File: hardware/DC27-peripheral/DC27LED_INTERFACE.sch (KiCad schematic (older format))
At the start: 16 parts, among them U2 IS31FL736

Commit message: commit the current hardware files
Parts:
- C1, C2, C3, C4, C5, C6, C7, C8, C9: footprint (none) -> Capacitor_SMD:C_0603_1608Metric
- R1, R2, R3, R4, R5, R6: footprint (none) -> Resistor_SMD:R_0603_1608Metric
- U2: footprint Package_DFN_QFN:QFN-40-1EP_4x4mm_P0.4mm_EP2.4x2.4mm -> dc27-sao-extras:QFN-40-1EP_5x5mm_P0.4mm_EP3.5x3.5mm
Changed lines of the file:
@@
 EESchema Schematic File Version 4
-LIBS:DC27-peripheral-cache
+LIBS:DC27-badge-cache
 EELAYER 26 0
 EELAYER END
@@
 F 0 "U2" H 5750 3450 50  0000 C CNN
 F 1 "IS31FL736" H 5750 3300 50  0000 C CNN
-F 2 "Package_DFN_QFN:QFN-40-1EP_4x4mm_P0.4mm_EP2.4x2.4mm" H 5700 1600 50  0001 C CNN
+F 2 "dc27-sao-extras:QFN-40-1EP_5x5mm_P0.4mm_EP3.5x3.5mm" H 5700 1600 50  0001 C CNN
 F 3 "http://www.issi.com/WW/pdf/IS31FL3216.pdf" H 4120 4590 50  0001 C CNN
 	1    5750 3450
@@
 F 0 "C1" H 2215 1496 50  0000 L CNN
 F 1 "0.47uF" H 2215 1405 50  0000 L CNN
-F 2 "" H 2138 1300 50  0001 C CNN
+F 2 "Capacitor_SMD:C_0603_1608Metric" H 2138 1300 50  0001 C CNN
 F 3 "~" H 2100 1450 50  0001 C CNN
 	1    2100 1450
@@
 F 0 "C2" H 2815 1496 50  0000 L CNN
 F 1 "0.1uF" H 2815 1405 50  0000 L CNN
-F 2 "" H 2738 1300 50  0001 C CNN
+F 2 "Capacitor_SMD:C_0603_1608Metric" H 2738 1300 50  0001 C CNN
 F 3 "~" H 2700 1450 50  0001 C CNN
 	1    2700 1450
@@
 F 0 "C3" H 2215 2496 50  0000 L CNN
 F 1 "0.47uF" H 2215 2405 50  0000 L CNN
-F 2 "" H 2138 2300 50  0001 C CNN
+F 2 "Capacitor_SMD:C_0603_1608Metric" H 2138 2300 50  0001 C CNN
 F 3 "~" H 2100 2450 50  0001 C CNN
 	1    2100 2450
@@
 F 0 "C4" H 2815 2496 50  0000 L CNN
 F 1 "0.1uF" H 2815 2405 50  0000 L CNN
-F 2 "" H 2738 2300 50  0001 C CNN
+F 2 "Capacitor_SMD:C_0603_1608Metric" H 2738 2300 50  0001 C CNN
 F 3 "~" H 2700 2450 50  0001 C CNN
 	1    2700 2450
@@
 F 0 "C5" H 2215 3496 50  0000 L CNN
 F 1 "0.47uF" H 2215 3405 50  0000 L CNN
-F 2 "" H 2138 3300 50  0001 C CNN
+F 2 "Capacitor_SMD:C_0603_1608Metric" H 2138 3300 50  0001 C CNN
 F 3 "~" H 2100 3450 50  0001 C CNN
 	1    2100 3450
@@
 F 0 "C6" H 2815 3496 50  0000 L CNN
 F 1 "0.1uF" H 2815 3405 50  0000 L CNN
-F 2 "" H 2738 3300 50  0001 C CNN
+F 2 "Capacitor_SMD:C_0603_1608Metric" H 2738 3300 50  0001 C CNN
 F 3 "~" H 2700 3450 50  0001 C CNN
 	1    2700 3450
@@
 F 0 "C7" H 2215 4496 50  0000 L CNN
 F 1 "0.47uF" H 2215 4405 50  0000 L CNN
-F 2 "" H 2138 4300 50  0001 C CNN
+F 2 "Capacitor_SMD:C_0603_1608Metric" H 2138 4300 50  0001 C CNN
 F 3 "~" H 2100 4450 50  0001 C CNN
 	1    2100 4450
@@
 F 0 "C8" H 2815 4496 50  0000 L CNN
 F 1 "0.1uF" H 2815 4405 50  0000 L CNN
-F 2 "" H 2738 4300 50  0001 C CNN
+F 2 "Capacitor_SMD:C_0603_1608Metric" H 2738 4300 50  0001 C CNN
 F 3 "~" H 2700 4450 50  0001 C CNN
 	1    2700 4450
@@
 F 0 "R5" V 7200 4250 50  0000 C CNN
 F 1 "20K" V 7300 4250 50  0000 C CNN
-F 2 "" V 7140 4240 50  0001 C CNN
+F 2 "Resistor_SMD:R_0603_1608Metric" V 7140 4240 50  0001 C CNN
 F 3 "~" H 7100 4250 50  0001 C CNN
 	1    7100 4250
@@
 F 0 "C9" H 2215 5546 50  0000 L CNN
 F 1 "C" H 2215 5455 50  0000 L CNN
-F 2 "" H 2138 5350 50  0001 C CNN
+F 2 "Capacitor_SMD:C_0603_1608Metric" H 2138 5350 50  0001 C CNN
 F 3 "~" H 2100 5500 50  0001 C CNN
 	1    2100 5500
@@
 F 0 "R6" H 5168 5196 50  0000 L CNN
 F 1 "100k" H 5168 5105 50  0000 L CNN
-F 2 "" V 5030 5150 50  0001 C CNN
+F 2 "Resistor_SMD:R_0603_1608Metric" V 5030 5150 50  0001 C CNN
 F 3 "~" H 5100 5150 50  0001 C CNN
 	1    5100 5150
@@
 F 0 "R1" H 8770 1496 50  0000 L CNN
 F 1 "100k" H 8770 1405 50  0000 L CNN
-F 2 "" V 8630 1450 50  0001 C CNN
+F 2 "Resistor_SMD:R_0603_1608Metric" V 8630 1450 50  0001 C CNN
 F 3 "~" H 8700 1450 50  0001 C CNN
 	1    8700 1450
@@
 F 0 "R2" H 9120 1496 50  0000 L CNN
 F 1 "1k" H 9120 1405 50  0000 L CNN
-F 2 "" V 8980 1450 50  0001 C CNN
+F 2 "Resistor_SMD:R_0603_1608Metric" V 8980 1450 50  0001 C CNN
 F 3 "~" H 9050 1450 50  0001 C CNN
 	1    9050 1450
@@
 F 0 "R3" H 9520 1496 50  0000 L CNN
 F 1 "1k" H 9520 1405 50  0000 L CNN
-F 2 "" V 9380 1450 50  0001 C CNN
+F 2 "Resistor_SMD:R_0603_1608Metric" V 9380 1450 50  0001 C CNN
 F 3 "~" H 9450 1450 50  0001 C CNN
 	1    9450 1450
@@
 F 0 "R4" H 9120 2996 50  0000 L CNN
 F 1 "100k" H 9120 2905 50  0000 L CNN
-F 2 "" V 8980 2950 50  0001 C CNN
+F 2 "Resistor_SMD:R_0603_1608Metric" V 8980 2950 50  0001 C CNN
 F 3 "~" H 9050 2950 50  0001 C CNN
 	1    9050 2950

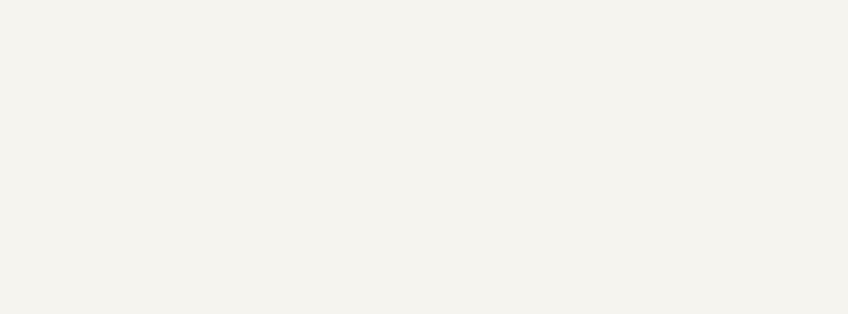
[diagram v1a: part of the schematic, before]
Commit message: Clean up SPI bus, set correct pins, start working through DRC errors.
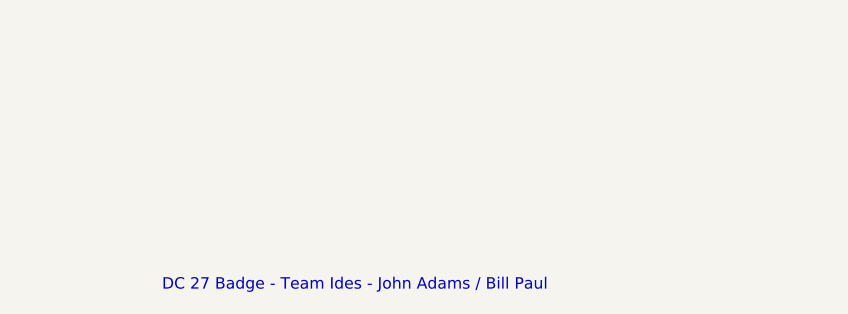
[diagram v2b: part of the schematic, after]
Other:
- note added: "DC 27 Badge - Team Ides - John Adams / Bill Paul"
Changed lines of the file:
@@
 Wire Wire Line
 	2100 5200 2700 5200
+Text Notes 7350 7500 0    50   ~ 0
+DC 27 Badge - Team Ides - John Adams / Bill Paul
 $EndSCHEMATC

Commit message: checkpoint all of the kicad stuff
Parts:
- renumbered C6 to C10, C7 to C11, C8 to C12, C9 to C13, C1 to C5, C2 to C6, C3 to C7, C4 to C8, C5 to C9, R1 to R3, R2 to R4, R3 to R5, R4 to R6, R5 to R7, R6 to R8, U2 to U3
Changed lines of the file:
@@
 $Descr A4 11693 8268
 encoding utf-8
-Sheet 3 5
+Sheet 3 6
 Title ""
 Date ""
@@
 P 5750 3450
 AR Path="/5BA1B02E/5BD866E6" Ref="U?"  Part="1"
-AR Path="/5BD866AF/5BD866E6" Ref="U2"  Part="1"
-F 0 "U2" H 5750 3450 50  0000 C CNN
+AR Path="/5BD866AF/5BD866E6" Ref="U3"  Part="1"
+F 0 "U3" H 5750 3450 50  0000 C CNN
 F 1 "IS31FL736" H 5750 3300 50  0000 C CNN
 F 2 "dc27-sao-extras:QFN-40-1EP_5x5mm_P0.4mm_EP3.5x3.5mm" H 5700 1600 50  0001 C CNN
@@
 VCC5V
 $Comp
-L Device:C C1
+L Device:C C5
 U 1 1 5BDAD420
 P 2100 1450
-F 0 "C1" H 2215 1496 50  0000 L CNN
+F 0 "C5" H 2215 1496 50  0000 L CNN
 F 1 "0.47uF" H 2215 1405 50  0000 L CNN
 F 2 "Capacitor_SMD:C_0603_1608Metric" H 2138 1300 50  0001 C CNN
@@
 $EndComp
 $Comp
-L Device:C C2
+L Device:C C6
 U 1 1 5BDAD49F
 P 2700 1450
-F 0 "C2" H 2815 1496 50  0000 L CNN
+F 0 "C6" H 2815 1496 50  0000 L CNN
 F 1 "0.1uF" H 2815 1405 50  0000 L CNN
 F 2 "Capacitor_SMD:C_0603_1608Metric" H 2738 1300 50  0001 C CNN
@@
 Connection ~ 2100 1250
 $Comp
-L power:GND #PWR04
+L power:GND #PWR017
 U 1 1 5BDADD7C
 P 2100 1800
-F 0 "#PWR04" H 2100 1550 50  0001 C CNN
+F 0 "#PWR017" H 2100 1550 50  0001 C CNN
 F 1 "GND" H 2105 1627 50  0000 C CNN
 F 2 "" H 2100 1800 50  0001 C CNN
@@
 $EndComp
 $Comp
-L power:GND #PWR05
+L power:GND #PWR018
 U 1 1 5BDADD94
 P 2700 1800
-F 0 "#PWR05" H 2700 1550 50  0001 C CNN
+F 0 "#PWR018" H 2700 1550 50  0001 C CNN
 F 1 "GND" H 2705 1627 50  0000 C CNN
 F 2 "" H 2700 1800 50  0001 C CNN
@@
 VCC5V
 $Comp
-L Device:C C3
+L Device:C C7
 U 1 1 5BDAF5E8
 P 2100 2450
-F 0 "C3" H 2215 2496 50  0000 L CNN
+F 0 "C7" H 2215 2496 50  0000 L CNN
 F 1 "0.47uF" H 2215 2405 50  0000 L CNN
 F 2 "Capacitor_SMD:C_0603_1608Metric" H 2138 2300 50  0001 C CNN
@@
 $EndComp
 $Comp
-L Device:C C4
+L Device:C C8
 U 1 1 5BDAF5EE
 P 2700 2450
-F 0 "C4" H 2815 2496 50  0000 L CNN
+F 0 "C8" H 2815 2496 50  0000 L CNN
 F 1 "0.1uF" H 2815 2405 50  0000 L CNN
 F 2 "Capacitor_SMD:C_0603_1608Metric" H 2738 2300 50  0001 C CNN
@@
 Connection ~ 2100 2250
 $Comp
-L power:GND #PWR06
+L power:GND #PWR019
 U 1 1 5BDAF5F9
 P 2100 2800
-F 0 "#PWR06" H 2100 2550 50  0001 C CNN
+F 0 "#PWR019" H 2100 2550 50  0001 C CNN
 F 1 "GND" H 2105 2627 50  0000 C CNN
 F 2 "" H 2100 2800 50  0001 C CNN
@@
 $EndComp
 $Comp
-L power:GND #PWR07
+L power:GND #PWR020
 U 1 1 5BDAF5FF
 P 2700 2800
-F 0 "#PWR07" H 2700 2550 50  0001 C CNN
+F 0 "#PWR020" H 2700 2550 50  0001 C CNN
 F 1 "GND" H 2705 2627 50  0000 C CNN
 F 2 "" H 2700 2800 50  0001 C CNN
@@
 VCC5V
 $Comp
-L Device:C C5
+L Device:C C9
 U 1 1 5BDAFD53
 P 2100 3450
-F 0 "C5" H 2215 3496 50  0000 L CNN
+F 0 "C9" H 2215 3496 50  0000 L CNN
 F 1 "0.47uF" H 2215 3405 50  0000 L CNN
 F 2 "Capacitor_SMD:C_0603_1608Metric" H 2138 3300 50  0001 C CNN
@@
 $EndComp
 $Comp
-L Device:C C6
+L Device:C C10
 U 1 1 5BDAFD59
 P 2700 3450
-F 0 "C6" H 2815 3496 50  0000 L CNN
+F 0 "C10" H 2815 3496 50  0000 L CNN
 F 1 "0.1uF" H 2815 3405 50  0000 L CNN
 F 2 "Capacitor_SMD:C_0603_1608Metric" H 2738 3300 50  0001 C CNN
@@
 Connection ~ 2100 3250
 $Comp
-L power:GND #PWR09
+L power:GND #PWR022
 U 1 1 5BDAFD64
 P 2100 3800
-F 0 "#PWR09" H 2100 3550 50  0001 C CNN
+F 0 "#PWR022" H 2100 3550 50  0001 C CNN
 F 1 "GND" H 2105 3627 50  0000 C CNN
 F 2 "" H 2100 3800 50  0001 C CNN
@@
 $EndComp
 $Comp
-L power:GND #PWR010
+L power:GND #PWR023
 U 1 1 5BDAFD6A
 P 2700 3800
-F 0 "#PWR010" H 2700 3550 50  0001 C CNN
+F 0 "#PWR023" H 2700 3550 50  0001 C CNN
 F 1 "GND" H 2705 3627 50  0000 C CNN
 F 2 "" H 2700 3800 50  0001 C CNN
@@
 VCC5V
 $Comp
-L Device:C C7
+L Device:C C11
 U 1 1 5BDAFD76
 P 2100 4450
-F 0 "C7" H 2215 4496 50  0000 L CNN
+F 0 "C11" H 2215 4496 50  0000 L CNN
 F 1 "0.47uF" H 2215 4405 50  0000 L CNN
 F 2 "Capacitor_SMD:C_0603_1608Metric" H 2138 4300 50  0001 C CNN
@@
 $EndComp
 $Comp
-L Device:C C8
+L Device:C C12
 U 1 1 5BDAFD7C
 P 2700 4450
-F 0 "C8" H 2815 4496 50  0000 L CNN
+F 0 "C12" H 2815 4496 50  0000 L CNN
 F 1 "0.1uF" H 2815 4405 50  0000 L CNN
 F 2 "Capacitor_SMD:C_0603_1608Metric" H 2738 4300 50  0001 C CNN
@@
 Connection ~ 2100 4250
 $Comp
-L power:GND #PWR012
+L power:GND #PWR025
 U 1 1 5BDAFD87
 P 2100 4800
-F 0 "#PWR012" H 2100 4550 50  0001 C CNN
+F 0 "#PWR025" H 2100 4550 50  0001 C CNN
 F 1 "GND" H 2105 4627 50  0000 C CNN
 F 2 "" H 2100 4800 50  0001 C CNN
@@
 $EndComp
 $Comp
-L power:GND #PWR013
+L power:GND #PWR026
 U 1 1 5BDAFD8D
 P 2700 4800
-F 0 "#PWR013" H 2700 4550 50  0001 C CNN
+F 0 "#PWR026" H 2700 4550 50  0001 C CNN
 F 1 "GND" H 2705 4627 50  0000 C CNN
 F 2 "" H 2700 4800 50  0001 C CNN
@@
 	5650 1850 5650 2100
 $Comp
-L power:GND #PWR03
+L power:GND #PWR016
 U 1 1 5BDB2F4A
 P 6050 1150
-F 0 "#PWR03" H 6050 900 50  0001 C CNN
+F 0 "#PWR016" H 6050 900 50  0001 C CNN
 F 1 "GND" H 6055 977 50  0000 C CNN
 F 2 "" H 6050 1150 50  0001 C CNN
@@
 	5950 1900 5950 2100
 $Comp
-L Device:R_US R5
+L Device:R_US R7
 U 1 1 5BDB589A
 P 7100 4250
-F 0 "R5" V 7200 4250 50  0000 C CNN
+F 0 "R7" V 7200 4250 50  0000 C CNN
 F 1 "20K" V 7300 4250 50  0000 C CNN
 F 2 "Resistor_SMD:R_0603_1608Metric" V 7140 4240 50  0001 C CNN
@@
 	6800 4250 6950 4250
 $Comp
-L power:GND #PWR011
+L power:GND #PWR024
 U 1 1 5BDB67EB
 P 7450 4300
-F 0 "#PWR011" H 7450 4050 50  0001 C CNN
+F 0 "#PWR024" H 7450 4050 50  0001 C CNN
 F 1 "GND" H 7455 4127 50  0000 C CNN
 F 2 "" H 7450 4300 50  0001 C CNN
@@
 VCC3V3
 $Comp
-L Device:C C9
+L Device:C C13
 U 1 1 5BDB89D2
 P 2100 5500
-F 0 "C9" H 2215 5546 50  0000 L CNN
+F 0 "C13" H 2215 5546 50  0000 L CNN
 F 1 "C" H 2215 5455 50  0000 L CNN
 F 2 "Capacitor_SMD:C_0603_1608Metric" H 2138 5350 50  0001 C CNN
@@
 $EndComp
 $Comp
-L power:GND #PWR015
+L power:GND #PWR028
 U 1 1 5BDB8A02
 P 2100 5750
-F 0 "#PWR015" H 2100 5500 50  0001 C CNN
+F 0 "#PWR028" H 2100 5500 50  0001 C CNN
 F 1 "GND" H 2105 5577 50  0000 C CNN
 F 2 "" H 2100 5750 50  0001 C CNN
@@
 NoConn ~ 6800 3150
 $Comp
-L power:GND #PWR014
+L power:GND #PWR027
 U 1 1 5BDBBD80
 P 5600 5600
-F 0 "#PWR014" H 5600 5350 50  0001 C CNN
+F 0 "#PWR027" H 5600 5350 50  0001 C CNN
 F 1 "GND" H 5605 5427 50  0000 C CNN
 F 2 "" H 5600 5600 50  0001 C CNN
@@
 Connection ~ 6000 5200
 $Comp
-L Device:R_US R6
+L Device:R_US R8
 U 1 1 5BDBF4DB
 P 5100 5150
-F 0 "R6" H 5168 5196 50  0000 L CNN
+F 0 "R8" H 5168 5196 50  0000 L CNN
 F 1 "100k" H 5168 5105 50  0000 L CNN
 F 2 "Resistor_SMD:R_0603_1608Metric" V 5030 5150 50  0001 C CNN
@@
 VCC3V3
 $Comp
-L Device:R R1
+L Device:R R3
 U 1 1 5BDEF0A9
 P 8700 1450
-F 0 "R1" H 8770 1496 50  0000 L CNN
+F 0 "R3" H 8770 1496 50  0000 L CNN
 F 1 "100k" H 8770 1405 50  0000 L CNN
 F 2 "Resistor_SMD:R_0603_1608Metric" V 8630 1450 50  0001 C CNN
@@
 $EndComp
 $Comp
-L Device:R R2
+L Device:R R4
 U 1 1 5BDEF0EE
 P 9050 1450
-F 0 "R2" H 9120 1496 50  0000 L CNN
+F 0 "R4" H 9120 1496 50  0000 L CNN
 F 1 "1k" H 9120 1405 50  0000 L CNN
 F 2 "Resistor_SMD:R_0603_1608Metric" V 8980 1450 50  0001 C CNN
@@
 $EndComp
 $Comp
-L Device:R R3
+L Device:R R5
 U 1 1 5BDEF141
 P 9450 1450
-F 0 "R3" H 9520 1496 50  0000 L CNN
+F 0 "R5" H 9520 1496 50  0000 L CNN
 F 1 "1k" H 9520 1405 50  0000 L CNN
 F 2 "Resistor_SMD:R_0603_1608Metric" V 9380 1450 50  0001 C CNN
@@
 	9450 2100 8550 2100
 $Comp
-L Device:R R4
+L Device:R R6
 U 1 1 5BE14E00
 P 9050 2950
-F 0 "R4" H 9120 2996 50  0000 L CNN
+F 0 "R6" H 9120 2996 50  0000 L CNN
 F 1 "100k" H 9120 2905 50  0000 L CNN
 F 2 "Resistor_SMD:R_0603_1608Metric" V 8980 2950 50  0001 C CNN
@@
 	9050 2350 8550 2350
 $Comp
-L power:GND #PWR08
+L power:GND #PWR021
 U 1 1 5BE17376
 P 9050 3250
-F 0 "#PWR08" H 9050 3000 50  0001 C CNN
+F 0 "#PWR021" H 9050 3000 50  0001 C CNN
 F 1 "GND" H 9055 3077 50  0000 C CNN
 F 2 "" H 9050 3250 50  0001 C CNN

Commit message: checkpoint everything - schematic passing DRC
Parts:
- removed R3, R6: 100k, Resistor_SMD:R_0603_1608Metric, symbol Device:R
- removed R4, R5: 1k, Resistor_SMD:R_0603_1608Metric, symbol Device:R
- removed U3: IS31FL736, dc27-sao-extras:QFN-40-1EP_5x5mm_P0.4mm_EP3.5x3.5mm, symbol Driver_LED:IS31FL736
- added R301: 10k, Resistor_SMD:R_0603_1608Metric, symbol Device:R
- added U301: IS31FL3216A, Package_DFN_QFN:QFN-40-1EP_5x5mm_P0.4mm_EP3.6x3.6mm, symbol DC27-badge-cache:IS31FL3216A
- C301: renamed from C5; value 0.47uF -> 1uF
- C303: renamed from C7; value 0.47uF -> 1uF
- C305: renamed from C9; value 0.47uF -> 1uF
- C307: renamed from C11; value 0.47uF -> 1uF
- C309: renamed from C13; value C -> 1uF
- R303: renamed from R8; value 100k -> 10k
- renumbered C6 to C302, C8 to C304, C10 to C306, C12 to C308, R7 to R302
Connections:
- net labels added: +3.3V, SCK_LED
- net labels removed: INTB_LED, INTB_MCU, SCB_LED, SCL_LED, SCL_MCU, SDA_MCU, SDB_LED, SDB_MCU, VCC3V3, VCC5V
- wire segments 103 -> 89
- no-connect marks 2 -> 3
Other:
- note added: "i2c addr 0xA0 (write) 0xA1 (read)\nchecked all pins 12/29"
- note removed: "I2C Bus Pullups"
